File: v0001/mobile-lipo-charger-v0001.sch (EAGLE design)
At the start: 31 parts, among them IC2 STM32F401VBT, SW1 DHT-4235A

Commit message: Added ADC Buffer
Added the ADC buffer and voltage divider for measuring the battery voltage before/during/after charging
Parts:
- added IC1, IC3: AD8610MR, analog-devices:AD8610MR
- added R5, R7: 1.5k, common:RES0603L3
- added R6, R8: 5.49k, common:RES0603L3
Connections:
- new net ADC_BUFF1: IC1.IN+, R5.1, R6.2
- new net ADC_BUFF2: IC3.IN+, R7.1, R8.2
- new net BATT1_V: IC1.IN-, IC1.OUT, IC2MCU.PA1
- new net BATT2_V: IC2MCU.PA2, IC3.IN-, IC3.OUT
- new net N$8: IC3.+VS
- new net N$9: IC1.+VS
- net BATT1_OUT: now also R5.2
- net BATT2_OUT: now also R7.2
- net GND: now also IC1.-VS, IC3.-VS, R6.1, R8.1
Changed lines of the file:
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@@
 <part name="BAT1" library="common" deviceset="KEYSTONE1048" device=""/>
 <part name="GND22" library="SparkFun-Aesthetics" deviceset="GND" device=""/>
+<part name="R5" library="common" deviceset="RES" device="0603L3" value="1.5k"/>
+<part name="R6" library="common" deviceset="RES" device="0603L3" value="5.49k"/>
+<part name="GND23" library="SparkFun-Aesthetics" deviceset="GND" device=""/>
+<part name="R7" library="common" deviceset="RES" device="0603L3" value="1.5k"/>
+<part name="R8" library="common" deviceset="RES" device="0603L3" value="5.49k"/>
+<part name="GND24" library="SparkFun-Aesthetics" deviceset="GND" device=""/>
+<part name="IC1" library="analog-devices" library_urn="urn:adsk.eagle:library:102" deviceset="AD8610" device="MR" package3d_urn="urn:adsk.eagle:package:3936/1"/>
+<part name="IC3" library="analog-devices" library_urn="urn:adsk.eagle:library:102" deviceset="AD8610" device="MR" package3d_urn="urn:adsk.eagle:package:3936/1"/>
+<part name="GND25" library="SparkFun-Aesthetics" deviceset="GND" device=""/>
+<part name="GND26" library="SparkFun-Aesthetics" deviceset="GND" device=""/>
 </parts>
 <sheets>
@@
 </segment>
 </net>
+<net name="BATT1_V" class="0">
+<segment>
+<pinref part="IC2" gate="MCU" pin="PA1"/>
+<wire x1="53.34" y1="-91.44" x2="53.34" y2="-76.2" width="0.1524" layer="91"/>
+<label x="53.34" y="-93.98" size="1.778" layer="95" rot="R90"/>
+</segment>
+</net>
+<net name="BATT2_V" class="0">
+<segment>
+<pinref part="IC2" gate="MCU" pin="PA2"/>
+<wire x1="55.88" y1="-91.44" x2="55.88" y2="-76.2" width="0.1524" layer="91"/>
+<label x="55.88" y="-93.98" size="1.778" layer="95" rot="R90"/>
+</segment>
+</net>
+</nets>
+</sheet>
+<sheet>
+<description>ADC Buffer</description>
+<plain>
+</plain>
+<instances>
+<instance part="R5" gate="G$1" x="68.58" y="78.74" smashed="yes" rot="R90">
+<attribute name="NAME" x="67.056" y="76.2" size="1.778" layer="95" rot="R90"/>
+<attribute name="VALUE" x="71.628" y="76.2" size="1.778" layer="96" rot="R90"/>
+</instance>
+<instance part="R6" gate="G$1" x="68.58" y="68.58" smashed="yes" rot="R90">
+<attribute name="NAME" x="67.056" y="66.04" size="1.778" layer="95" rot="R90"/>
+<attribute name="VALUE" x="71.628" y="66.04" size="1.778" layer="96" rot="R90"/>
+</instance>
+<instance part="GND23" gate="1" x="68.58" y="60.96" smashed="yes">
+<attribute name="VALUE" x="66.04" y="58.42" size="1.778" layer="96"/>
+</instance>
+<instance part="R7" gate="G$1" x="68.58" y="25.4" smashed="yes" rot="R90">
+<attribute name="NAME" x="67.056" y="22.86" size="1.778" layer="95" rot="R90"/>
+<attribute name="VALUE" x="71.628" y="22.86" size="1.778" layer="96" rot="R90"/>
+</instance>
+<instance part="R8" gate="G$1" x="68.58" y="15.24" smashed="yes" rot="R90">
+<attribute name="NAME" x="67.056" y="12.7" size="1.778" layer="95" rot="R90"/>
+<attribute name="VALUE" x="71.628" y="12.7" size="1.778" layer="96" rot="R90"/>
+</instance>
+<instance part="GND24" gate="1" x="68.58" y="7.62" smashed="yes">
+<attribute name="VALUE" x="66.04" y="5.08" size="1.778" layer="96"/>
+</instance>
+<instance part="IC1" gate="G$1" x="104.14" y="71.12" smashed="yes">
+<attribute name="NAME" x="111.76" y="73.66" size="1.778" layer="95"/>
+<attribute name="VALUE" x="111.76" y="67.31" size="1.778" layer="96"/>
+</instance>
+<instance part="IC3" gate="G$1" x="104.14" y="17.78" smashed="yes">
+<attribute name="NAME" x="111.76" y="20.32" size="1.778" layer="95"/>
+<attribute name="VALUE" x="111.76" y="13.97" size="1.778" layer="96"/>
+</instance>
+<instance part="GND25" gate="1" x="104.14" y="50.8" smashed="yes">
+<attribute name="VALUE" x="101.6" y="48.26" size="1.778" layer="96"/>
+</instance>
+<instance part="GND26" gate="1" x="104.14" y="-2.54" smashed="yes">
+<attribute name="VALUE" x="101.6" y="-5.08" size="1.778" layer="96"/>
+</instance>
+</instances>
+<busses>
+</busses>
+<nets>
+<net name="BATT1_OUT" class="0">
+<segment>
+<pinref part="R5" gate="G$1" pin="2"/>
+<wire x1="68.58" y1="81.28" x2="68.58" y2="96.52" width="0.1524" layer="91"/>
+<label x="71.12" y="86.36" size="1.778" layer="95" rot="R90"/>
+</segment>
+</net>
+<net name="ADC_BUFF1" class="0">
+<segment>
+<pinref part="R5" gate="G$1" pin="1"/>
+<pinref part="R6" gate="G$1" pin="2"/>
+<wire x1="68.58" y1="76.2" x2="68.58" y2="73.66" width="0.1524" layer="91"/>
+<wire x1="68.58" y1="73.66" x2="68.58" y2="71.12" width="0.1524" layer="91"/>
+<junction x="68.58" y="73.66"/>
+<label x="73.66" y="71.12" size="1.778" layer="95"/>
+<pinref part="IC1" gate="G$1" pin="IN+"/>
+<wire x1="99.06" y1="73.66" x2="68.58" y2="73.66" width="0.1524" layer="91"/>
+</segment>
+</net>
+<net name="GND" class="0">
+<segment>
+<pinref part="R6" gate="G$1" pin="1"/>
+<wire x1="68.58" y1="66.04" x2="68.58" y2="63.5" width="0.1524" layer="91"/>
+<pinref part="GND23" gate="1" pin="GND"/>
+</segment>
+<segment>
+<pinref part="R8" gate="G$1" pin="1"/>
+<pinref part="GND24" gate="1" pin="GND"/>
+<wire x1="68.58" y1="10.16" x2="68.58" y2="12.7" width="0.1524" layer="91"/>
+</segment>
+<segment>
+<pinref part="IC1" gate="G$1" pin="-VS"/>
+<wire x1="104.14" y1="60.96" x2="104.14" y2="53.34" width="0.1524" layer="91"/>
+<pinref part="GND25" gate="1" pin="GND"/>
+</segment>
+<segment>
+<pinref part="IC3" gate="G$1" pin="-VS"/>
+<wire x1="104.14" y1="7.62" x2="104.14" y2="0" width="0.1524" layer="91"/>
+<pinref part="GND26" gate="1" pin="GND"/>
+</segment>
+</net>
+<net name="ADC_BUFF2" class="0">
+<segment>
+<pinref part="R8" gate="G$1" pin="2"/>
+<pinref part="R7" gate="G$1" pin="1"/>
+<wire x1="68.58" y1="17.78" x2="68.58" y2="20.32" width="0.1524" layer="91"/>
+<wire x1="68.58" y1="20.32" x2="68.58" y2="22.86" width="0.1524" layer="91"/>
+<junction x="68.58" y="20.32"/>
+<label x="73.66" y="17.78" size="1.778" layer="95"/>
+<pinref part="IC3" gate="G$1" pin="IN+"/>
+<wire x1="99.06" y1="20.32" x2="68.58" y2="20.32" width="0.1524" layer="91"/>
+</segment>
+</net>
+<net name="BATT2_OUT" class="0">
+<segment>
+<pinref part="R7" gate="G$1" pin="2"/>
+<wire x1="68.58" y1="27.94" x2="68.58" y2="43.18" width="0.1524" layer="91"/>
+<label x="71.12" y="33.02" size="1.778" layer="95" rot="R90"/>
+</segment>
+</net>
+<net name="BATT2_V" class="0">
+<segment>
+<pinref part="IC3" gate="G$1" pin="OUT"/>
+<wire x1="114.3" y1="17.78" x2="127" y2="17.78" width="0.1524" layer="91"/>
+<wire x1="127" y1="17.78" x2="127" y2="2.54" width="0.1524" layer="91"/>
+<wire x1="127" y1="2.54" x2="96.52" y2="2.54" width="0.1524" layer="91"/>
+<wire x1="96.52" y1="2.54" x2="96.52" y2="15.24" width="0.1524" layer="91"/>
+<pinref part="IC3" gate="G$1" pin="IN-"/>
+<wire x1="96.52" y1="15.24" x2="99.06" y2="15.24" width="0.1524" layer="91"/>
+<wire x1="137.16" y1="17.78" x2="127" y2="17.78" width="0.1524" layer="91"/>
+<junction x="127" y="17.78"/>
+<label x="129.54" y="15.24" size="1.778" layer="95"/>
+</segment>
+</net>
+<net name="BATT1_V" class="0">
+<segment>
+<pinref part="IC1" gate="G$1" pin="OUT"/>
+<wire x1="114.3" y1="71.12" x2="127" y2="71.12" width="0.1524" layer="91"/>
+<wire x1="127" y1="71.12" x2="127" y2="55.88" width="0.1524" layer="91"/>
+<wire x1="127" y1="55.88" x2="96.52" y2="55.88" width="0.1524" layer="91"/>
+<wire x1="96.52" y1="55.88" x2="96.52" y2="68.58" width="0.1524" layer="91"/>
+<pinref part="IC1" gate="G$1" pin="IN-"/>
+<wire x1="96.52" y1="68.58" x2="99.06" y2="68.58" width="0.1524" layer="91"/>
+<wire x1="137.16" y1="71.12" x2="127" y2="71.12" width="0.1524" layer="91"/>
+<junction x="127" y="71.12"/>
+<label x="129.54" y="68.58" size="1.778" layer="95"/>
+</segment>
+</net>
+<net name="N$8" class="0">
+<segment>
+<pinref part="IC3" gate="G$1" pin="+VS"/>
+<wire x1="104.14" y1="38.1" x2="104.14" y2="27.94" width="0.1524" layer="91"/>
+</segment>
+</net>
+<net name="N$9" class="0">
+<segment>
+<pinref part="IC1" gate="G$1" pin="+VS"/>
+<wire x1="104.14" y1="91.44" x2="104.14" y2="81.28" width="0.1524" layer="91"/>
+</segment>
+</net>

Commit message: Added buffers
Added the buffers to the ADC for the MCU and laid out the board for those parts.
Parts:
- added JP1: (no value), pinhead:PINHD-2X5
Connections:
- new net TCK_SWCLK: IC2MCU.PA14, JP1.4
- new net TMS_SWDIO: IC2MCU.PA13, JP1.2
- net BATT1_V: now also IC2MCU.PA2; no longer IC2MCU.PA1
- net BATT2_V: now also IC2MCU.PA1; no longer IC2MCU.PA2
- net GND: now also JP1.3, JP1.5, JP1.9
- net RST: now also JP1.10
- net VDD: now also JP1.1
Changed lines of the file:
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@@
 <part name="GND25" library="SparkFun-Aesthetics" deviceset="GND" device=""/>
 <part name="GND26" library="SparkFun-Aesthetics" deviceset="GND" device=""/>
+<part name="JP1" library="pinhead" library_urn="urn:adsk.eagle:library:325" deviceset="PINHD-2X5" device="" package3d_urn="urn:adsk.eagle:package:22470/2"/>
+<part name="GND27" library="SparkFun-Aesthetics" deviceset="GND" device=""/>
+<part name="SUPPLY4" library="SparkFun-PowerSymbols" library_urn="urn:adsk.eagle:library:530" deviceset="VDD" device=""/>
 </parts>
 <sheets>
@@
 <instance part="GND21" gate="1" x="20.32" y="-76.2" smashed="yes">
 <attribute name="VALUE" x="17.78" y="-78.74" size="1.778" layer="96"/>
+</instance>
+<instance part="JP1" gate="A" x="-71.12" y="-12.7" smashed="yes">
+<attribute name="NAME" x="-77.47" y="-4.445" size="1.778" layer="95"/>
+<attribute name="VALUE" x="-77.47" y="-22.86" size="1.778" layer="96"/>
+</instance>
+<instance part="GND27" gate="1" x="-91.44" y="-22.86" smashed="yes">
+<attribute name="VALUE" x="-93.98" y="-25.4" size="1.778" layer="96"/>
+</instance>
+<instance part="SUPPLY4" gate="VDD" x="-91.44" y="-5.08" smashed="yes">
+<attribute name="VALUE" x="-91.44" y="-2.286" size="1.778" layer="96" align="bottom-center"/>
 </instance>
 </instances>
@@
 <pinref part="R4" gate="G$1" pin="1"/>
 <pinref part="GND21" gate="1" pin="GND"/>
+</segment>
+<segment>
+<pinref part="JP1" gate="A" pin="3"/>
+<wire x1="-73.66" y1="-10.16" x2="-91.44" y2="-10.16" width="0.1524" layer="91"/>
+<pinref part="JP1" gate="A" pin="5"/>
+<wire x1="-73.66" y1="-12.7" x2="-91.44" y2="-12.7" width="0.1524" layer="91"/>
+<wire x1="-91.44" y1="-10.16" x2="-91.44" y2="-12.7" width="0.1524" layer="91"/>
+<pinref part="JP1" gate="A" pin="9"/>
+<wire x1="-73.66" y1="-17.78" x2="-91.44" y2="-17.78" width="0.1524" layer="91"/>
+<wire x1="-91.44" y1="-12.7" x2="-91.44" y2="-17.78" width="0.1524" layer="91"/>
+<junction x="-91.44" y="-12.7"/>
+<wire x1="-91.44" y1="-17.78" x2="-91.44" y2="-20.32" width="0.1524" layer="91"/>
+<junction x="-91.44" y="-17.78"/>
+<pinref part="GND27" gate="1" pin="GND"/>
 </segment>
 </net>
@@
 <wire x1="-35.56" y1="-63.5" x2="-35.56" y2="-60.96" width="0.1524" layer="91"/>
 </segment>
+<segment>
+<pinref part="JP1" gate="A" pin="1"/>
+<wire x1="-73.66" y1="-7.62" x2="-91.44" y2="-7.62" width="0.1524" layer="91"/>
+<wire x1="-91.44" y1="-5.08" x2="-91.44" y2="-7.62" width="0.1524" layer="91"/>
+<pinref part="SUPPLY4" gate="VDD" pin="VDD"/>
+</segment>
 </net>
 <net name="N$3" class="0">
@@
 <pinref part="R2" gate="G$1" pin="2"/>
 <label x="38.1" y="-50.8" size="1.778" layer="95"/>
+</segment>
+<segment>
+<pinref part="JP1" gate="A" pin="10"/>
+<wire x1="-48.26" y1="-17.78" x2="-66.04" y2="-17.78" width="0.1524" layer="91"/>
+<label x="-60.96" y="-17.78" size="1.778" layer="95"/>
 </segment>
 </net>
@@
 </segment>
 </net>
-<net name="BATT1_V" class="0">
+<net name="BATT2_V" class="0">
 <segment>
 <pinref part="IC2" gate="MCU" pin="PA1"/>
@@
 </segment>
 </net>
-<net name="BATT2_V" class="0">
+<net name="TMS_SWDIO" class="0">
+<segment>
+<pinref part="JP1" gate="A" pin="2"/>
+<wire x1="-66.04" y1="-7.62" x2="-48.26" y2="-7.62" width="0.1524" layer="91"/>
+<label x="-60.96" y="-7.62" size="1.778" layer="95"/>
+</segment>
+<segment>
+<pinref part="IC2" gate="MCU" pin="PA13"/>
+<wire x1="83.82" y1="-91.44" x2="83.82" y2="-76.2" width="0.1524" layer="91"/>
+<label x="83.82" y="-93.98" size="1.778" layer="95" rot="R90"/>
+</segment>
+</net>
+<net name="TCK_SWCLK" class="0">
+<segment>
+<pinref part="JP1" gate="A" pin="4"/>
+<wire x1="-48.26" y1="-10.16" x2="-66.04" y2="-10.16" width="0.1524" layer="91"/>
+<label x="-60.96" y="-10.16" size="1.778" layer="95"/>
+</segment>
+<segment>
+<pinref part="IC2" gate="MCU" pin="PA14"/>
+<wire x1="86.36" y1="-91.44" x2="86.36" y2="-76.2" width="0.1524" layer="91"/>
+<label x="86.36" y="-93.98" size="1.778" layer="95" rot="R90"/>
+</segment>
+</net>
+<net name="BATT1_V" class="0">
 <segment>
 <pinref part="IC2" gate="MCU" pin="PA2"/>
@@
 </nets>
 </sheet>
+<sheet>
+<plain>
+</plain>
+<instances>
+</instances>
+<busses>
+</busses>
+<nets>
+</nets>
+</sheet>

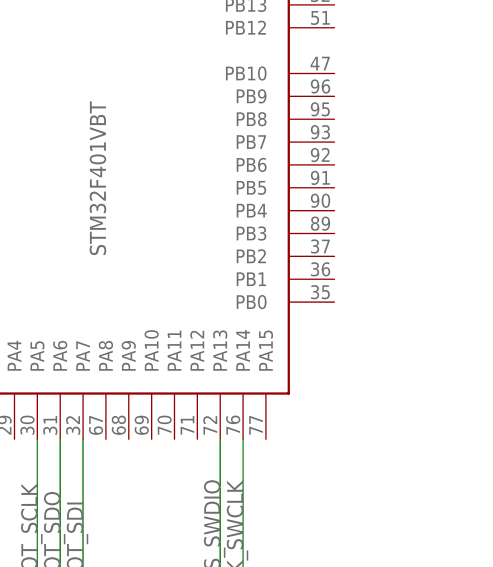
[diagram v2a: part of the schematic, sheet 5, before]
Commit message: Charger Chip Enable
Routed the charger chip enable lines.
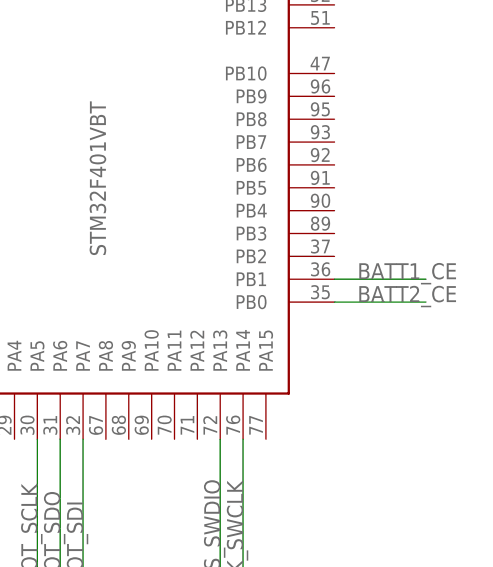
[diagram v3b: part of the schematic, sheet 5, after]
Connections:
- net BATT1_CE: now also IC2MCU.PB1
- net BATT2_CE: now also IC2MCU.PB0
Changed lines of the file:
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@@
+</segment>
+</net>
+<net name="BATT2_CE" class="0">
+<segment>
+<pinref part="IC2" gate="MCU" pin="PB0"/>
+<wire x1="106.68" y1="-60.96" x2="96.52" y2="-60.96" width="0.1524" layer="91"/>
+<label x="99.06" y="-60.96" size="1.778" layer="95"/>
+</segment>
+</net>
+<net name="BATT1_CE" class="0">
+<segment>
+<pinref part="IC2" gate="MCU" pin="PB1"/>
+<wire x1="106.68" y1="-58.42" x2="96.52" y2="-58.42" width="0.1524" layer="91"/>
+<label x="99.06" y="-58.42" size="1.778" layer="95"/>
 </segment>
 </net>
